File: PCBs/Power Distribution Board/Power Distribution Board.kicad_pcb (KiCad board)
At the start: 2 copper layers, 60 x 85 mm, 110 parts, among them J1 Conn_01x01, J10 Conn_01x01, J11 Conn_01x01, J12 Conn_01x01, J13 Conn_01x01, J14 Conn_01x01, J15 Conn_01x01, J16 Conn_01x01, J17 Conn_01x01, J18 Conn_01x01, J19 Conn_01x01, J2 Conn_01x01, J20 Conn_01x01, J21 Conn_01x01, J22 Conn_01x01, J23 Conn_01x01, J24 Conn_01x01, J25 Conn_01x01, J26 Conn_01x01, J27 Conn_01x01, J28 USB_B_Mini, J29 Conn_02x05_Odd_Even, J3 Conn_01x01, J4 Conn_01x01, J5 Conn_01x01, J6 Conn_01x01, J7 Conn_01x01, J8 Conn_01x01, J9 Conn_01x01, SW1 SW_Push, U1 ACS711, U10 ACS711, U11 TLV733P, U12 ATSAMD21E16L-MFT, U2 ACS711, U3 ACS711, U4 ACS711, U5 ACS711, U6 ACS711, U7 ACS711, U8 ACS711, U9 ACS711, Y1 32.7680kHz

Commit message: Initial Routing Finalized
Power Distribution Board is pretty much ready to go. Need to fix up the silkscreen and touch up routing but that will take only a little bit of time.
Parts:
- moved C22 15.8 mm to (112.1, 21.9), turned to 180 degrees
- moved J29 13.9 mm to (119.7, 18.2), turned to 90 degrees
- moved C38 13.3 mm to (110.7, 18.7)
- moved Y1 13.3 mm to (113.8, 18.6)
- moved C37 13.3 mm to (113.0, 16.5)
- moved U12 13.1 mm to (118.7, 23.5)
- moved C32 13.0 mm to (125.4, 35.5)
- moved C25 12.8 mm to (112.1, 23.3), turned to 180 degrees
- moved C34 12.5 mm to (127.3, 35.2), turned to 270 degrees
- moved C35 11.4 mm to (112.1, 26.1), turned to 180 degrees
- moved C31 10.7 mm to (112.1, 24.7), turned to 180 degrees
- moved R14 9.97 mm to (124.8, 23.4), turned to 90 degrees
- moved C39 9.61 mm to (112.2, 27.4), turned to 180 degrees
- moved SW1 9.23 mm to (134.8, 17.6), turned to 180 degrees
- moved C36 8.42 mm to (116.3, 28.8), turned to 270 degrees
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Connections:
- U12 pad 11: VIOUT7 -> VIOUT8
- U12 pad 12: VIOUT8 -> VIOUT6
- U12 pad 13: VIOUT9 -> VIOUT4
- U12 pad 14: VIOUT10 -> VIOUT2
- U12 pad 33: (no net) -> GND
- U12 pad 4: VIOUT2 -> VIOUT3
- U12 pad 5: VIOUT3 -> VIOUT5
- U12 pad 6: VIOUT4 -> VIOUT7
- U12 pad 7: VIOUT5 -> VIOUT9
- U12 pad 8: VIOUT6 -> VIOUT10
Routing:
- net +3V3: track 0.00 -> 250.5 mm, vias 0 -> 13
- net GND: track 0.00 -> 158.8 mm, vias 0 -> 40
- net VIOUT9: track 0.00 -> 78.6 mm, vias 0 -> 2
- net VIOUT7: track 0.00 -> 71.1 mm, vias 0 -> 2
- net VIOUT10: track 0.00 -> 68.5 mm, vias 0 -> 2
- net VIOUT5: track 0.00 -> 63.0 mm, vias 0 -> 2
- net VIOUT8: track 0.00 -> 56.9 mm, vias 0 -> 2
- net VIOUT3: track 0.00 -> 54.9 mm, vias 0 -> 2
- net VIOUT6: track 0.00 -> 47.5 mm, vias 0 -> 2
- net VIOUT1: track 0.00 -> 45.3 mm, vias 0 -> 2
- net VIOUT4: track 0.00 -> 38.8 mm, vias 0 -> 2
- net USB-: track 0.00 -> 34.7 mm
- net USB+: track 0.00 -> 33.8 mm
- net VIOUT2: track 0.00 -> 29.6 mm, vias 0 -> 2
- net ~RESET: track 0.00 -> 21.8 mm, vias 0 -> 3
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- added copper zone on F.Cu, net +3V3
- added copper zone on F.Cu, net +5V
- added copper zone on F.Cu, net 12V_IN
- added copper zone on F.Cu, net 12V_OUT1
- added copper zone on F.Cu, net 12V_OUT10
- added copper zone on F.Cu, net 12V_OUT2
- added copper zone on F.Cu, net 12V_OUT3
- added copper zone on F.Cu, net 12V_OUT4
- added copper zone on F.Cu, net 12V_OUT5
- added copper zone on F.Cu, net 12V_OUT6
- added copper zone on F.Cu, net 12V_OUT7
- added copper zone on F.Cu, net 12V_OUT8
- added copper zone on F.Cu, net 12V_OUT9
- added copper zone on F.Cu, net 3V3_FILT
- added copper zone on B.Cu, net GND
- added copper zone on F.Cu, net GND
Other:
- net class Default: via_dia 0.8 -> 0.6; via_drill 0.4 -> 0.3

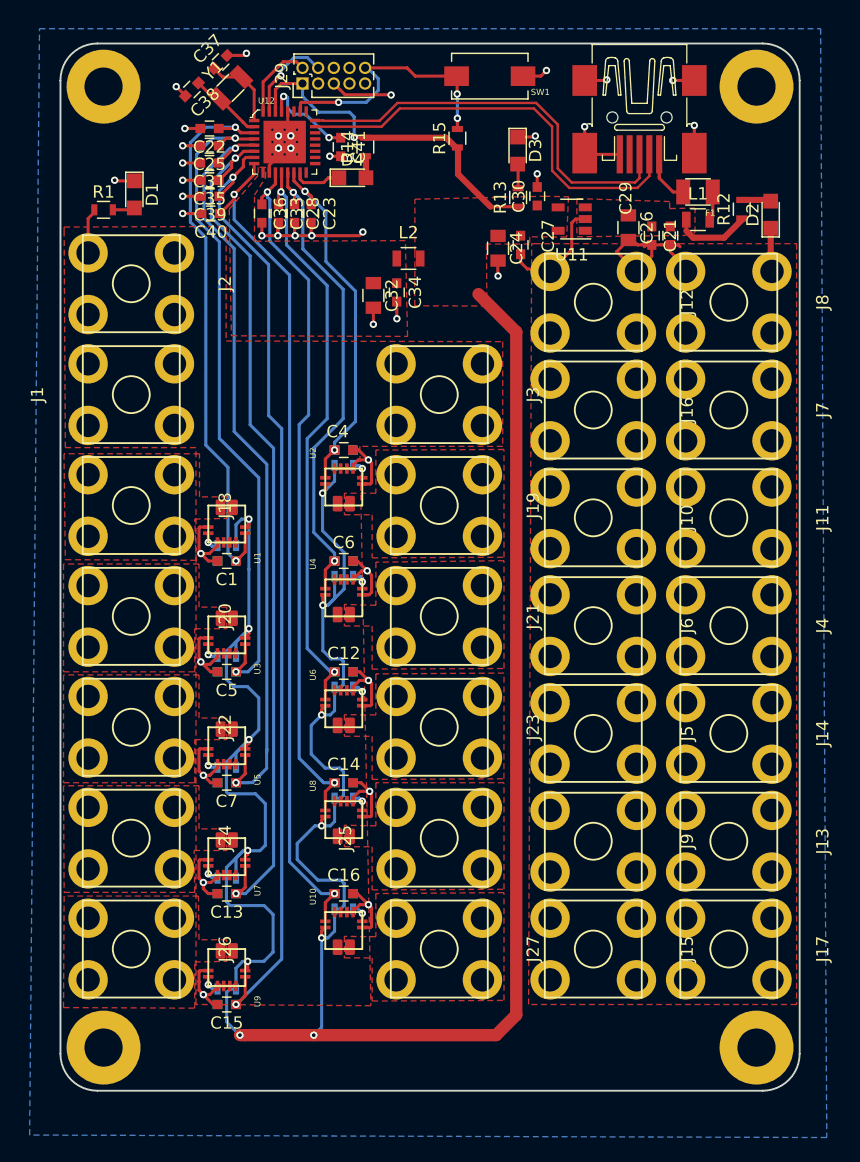
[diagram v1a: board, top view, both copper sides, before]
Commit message: Updated Silkscreen PD
Still need to check over the layout one last time, but she should be good to go.
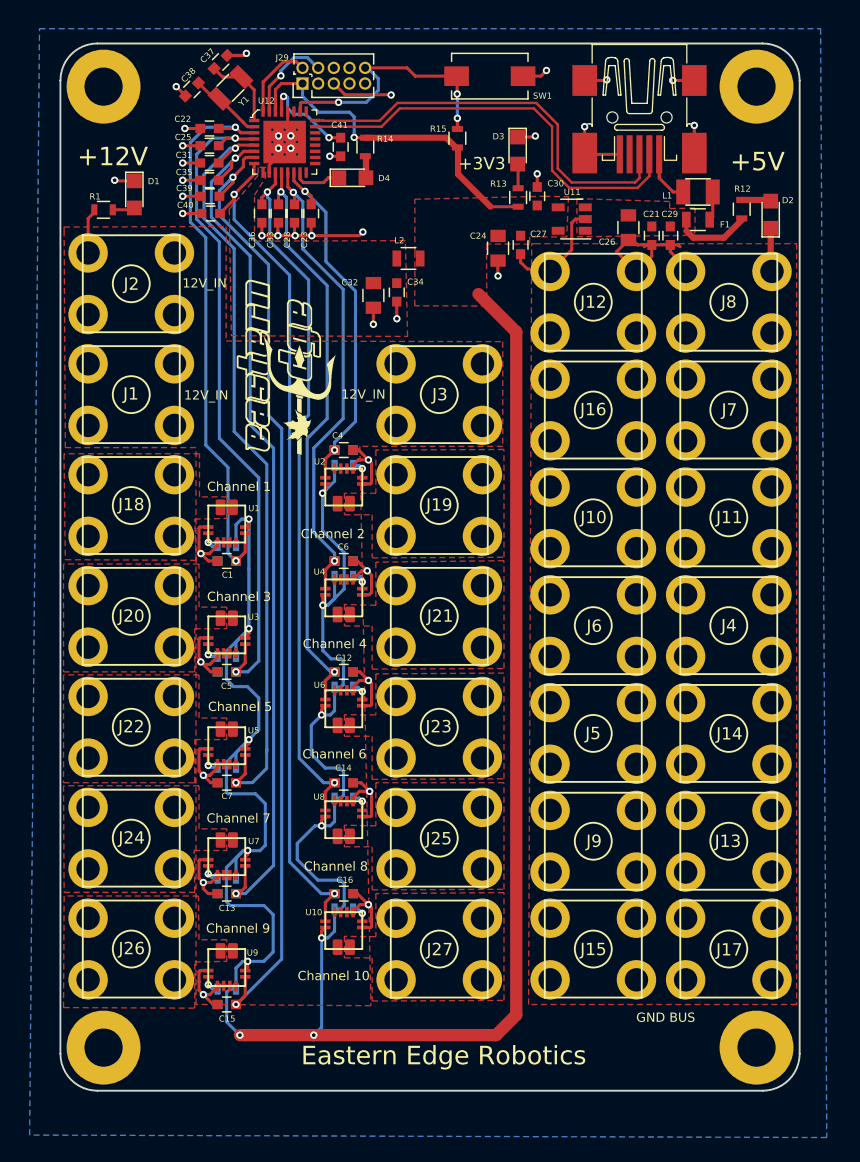
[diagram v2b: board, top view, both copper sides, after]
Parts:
- added U$12: EERLOGO, EER:EERLOGO, F.Cu at (124.1, 50.9)
- added U$14: EERLOGOLONG, EER:EERLOGOLONG, B.Cu at (113.6, 96.8)
- added U$15: MUNLOGO, EER:MUNLOGO, B.Cu at (160.9, 32.6)
- added U$16: MILOGO, EER:MILOGO, B.Cu at (142.6, 32.8)
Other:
- board text added: "+12V"
- board text added: "+3V3"
- board text added: "+5V"
- board text added: "12V_IN"
- board text added: "Channel 1"
- board text added: "Channel 10"
- board text added: "Channel 2"
- board text added: "Channel 3"
- board text added: "Channel 4"
- board text added: "Channel 5"
- board text added: "Channel 6"
- board text added: "Channel 7"
- board text added: "Channel 8"
- board text added: "Channel 9"
- board text added: "Eastern Edge Robotics"
- board text added: "GND BUS"
- board text added: "Mark Belbin -- 2018"
- board text added: "Power Distribution Board"
